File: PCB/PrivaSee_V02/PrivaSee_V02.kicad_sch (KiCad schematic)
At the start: 35 parts, among them J1 RFPC-SMA27-F, J2 Batt_Solder_Point, J3 Conn_02x06_Odd_Even, J4 VOUT_TEST, J5 GND_TEST, J6 IR_TEST, J7 RF_TEST, SW1 Switch, SW2 SW_Push, U1 RC1602A, U2 LM358, U3 254, U4 DFR0568, U6 ESP32-C5-DevKitC-1

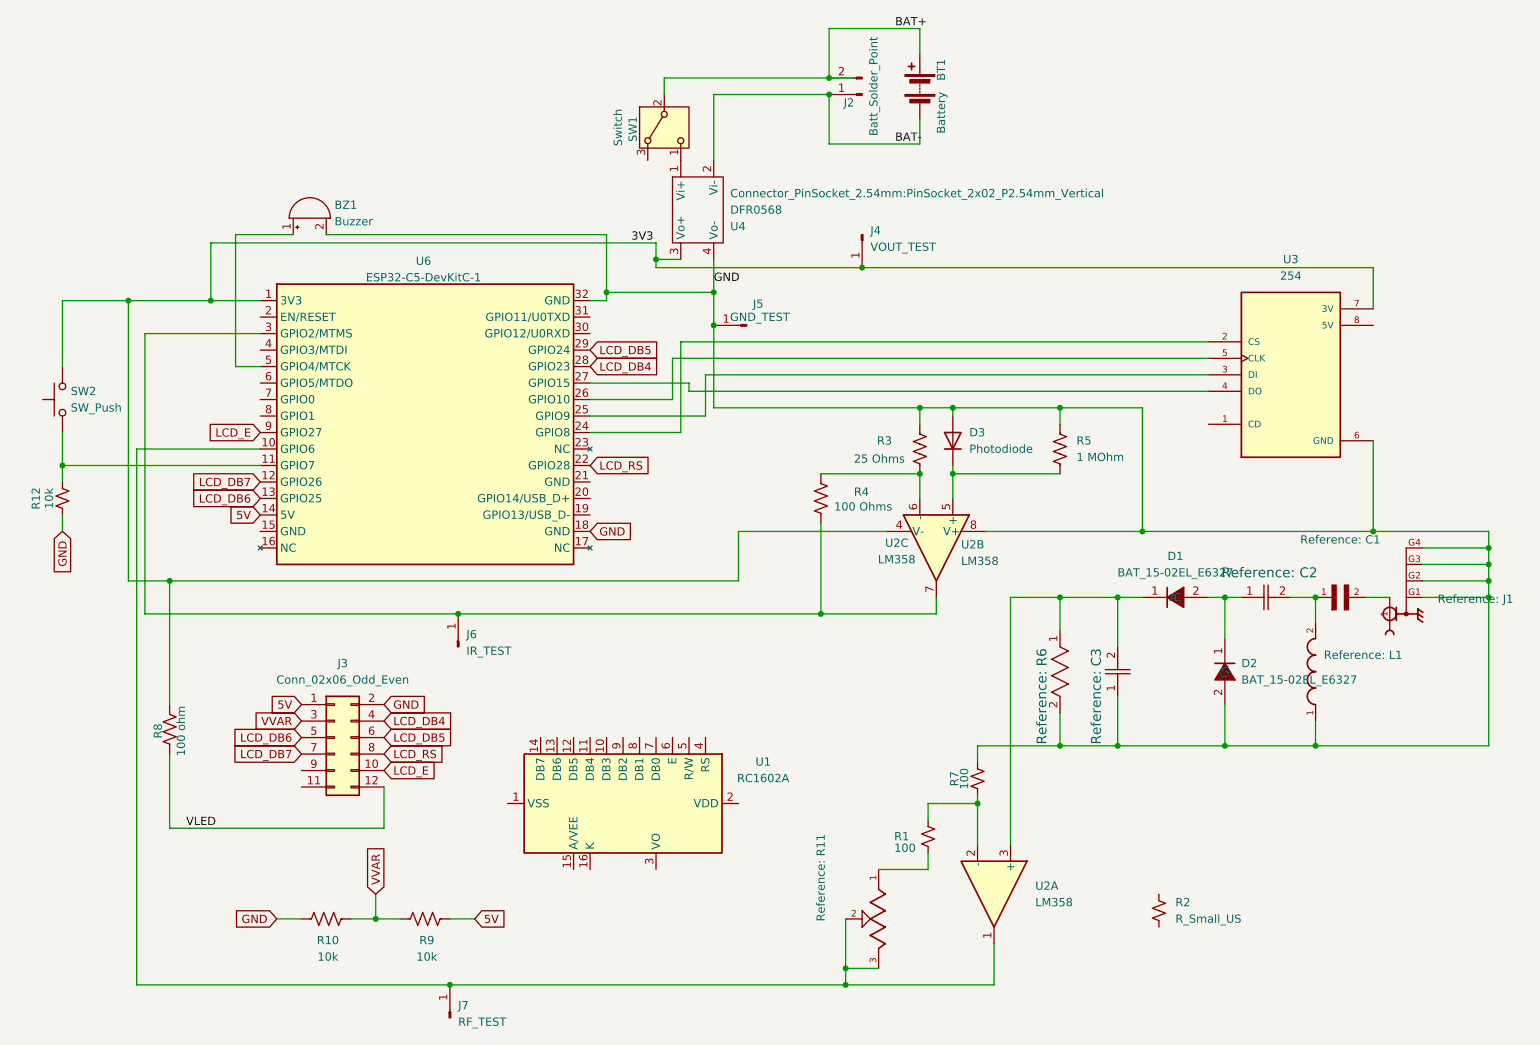
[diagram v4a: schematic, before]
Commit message: capacitor replacement
handsolderable foot print
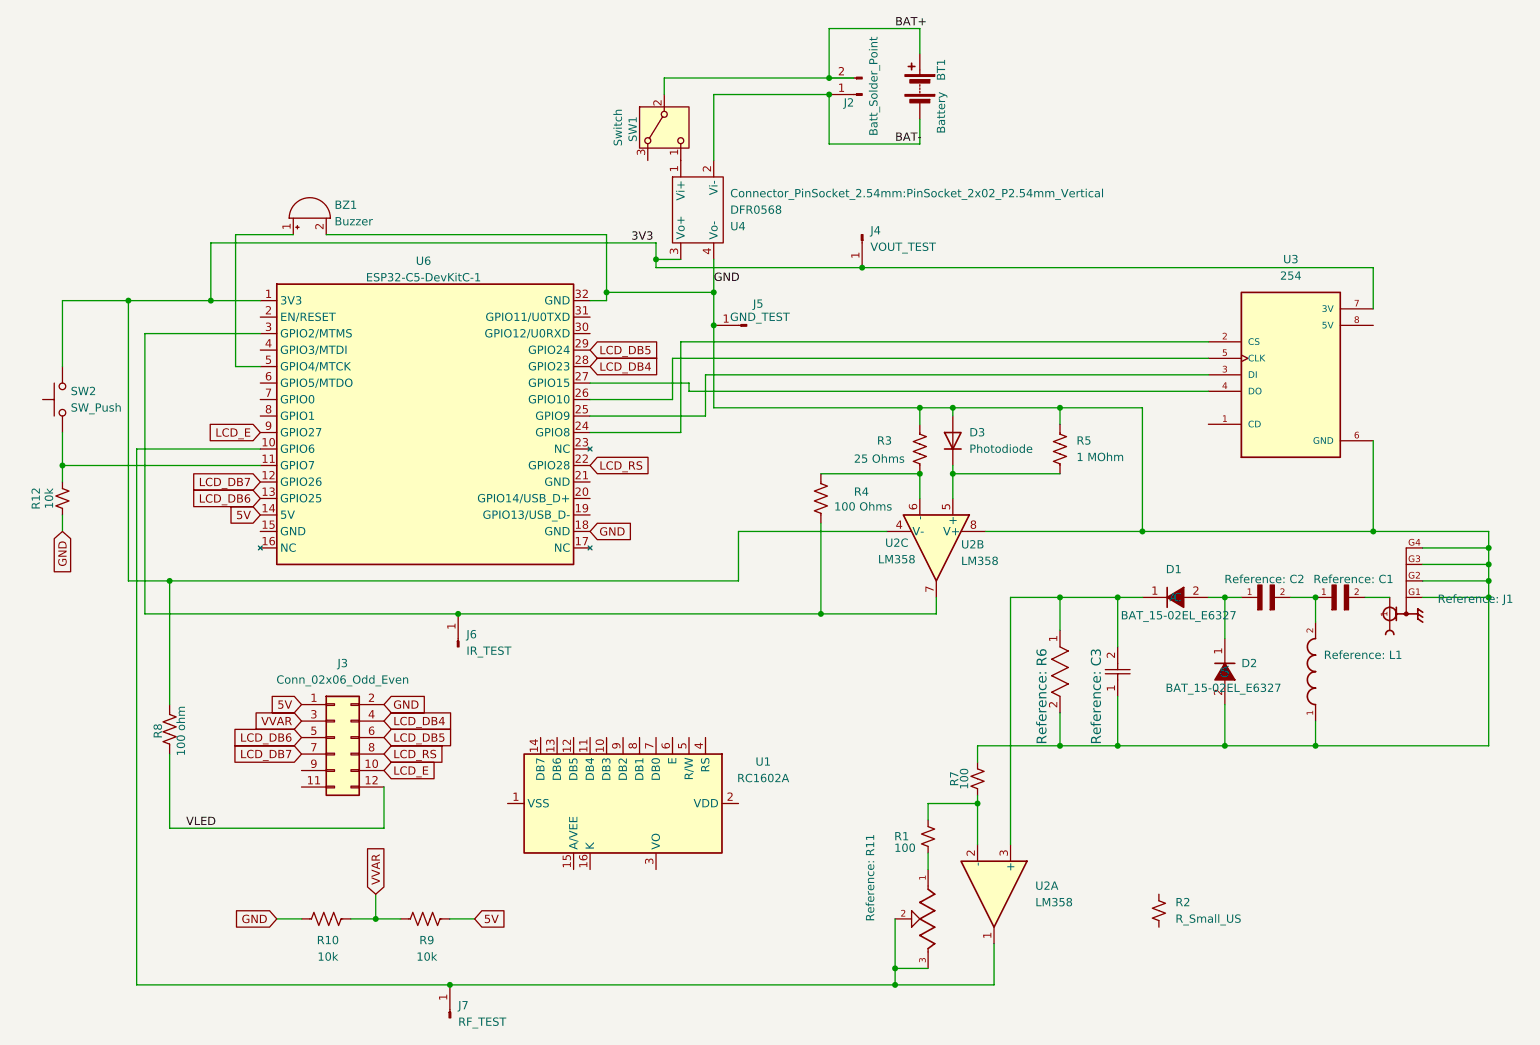
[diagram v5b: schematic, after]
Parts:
- removed C2: GJM1555C1H4R7CB01D, Snapeda:G-155_MUR-L, symbol Snapeda:GJM1555C1H4R7CB01D
- added C2: GJM1555C1H4R7BB01D, Snapeda:CAPC1005X55N, symbol Snapeda:GJM1555C1H4R7BB01D
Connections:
- net at D1.2 (A), D2.1 (C): now also C2.1
- net at C1.1, L1.2: now also C2.2
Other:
- moved on the sheet: Reference: R11
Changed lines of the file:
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@@
 	)
 	(junction
-		(at 154.94 162.56)
-		(diameter 0)
-		(color 0 0 0 0)
-	)
-	(junction
 		(at 213.36 102.87)
 		(diameter 0)
@@
 	)
 	(junction
-		(at 154.94 160.02)
+		(at 44.45 57.15)
 		(diameter 0)
 		(color 0 0 0 0)
 	)
 	(junction
-		(at 44.45 57.15)
+		(at 162.56 160.02)
 		(diameter 0)
 		(color 0 0 0 0)
@@
 		(color 0 0 0 0)
 	)
+	(junction
+		(at 162.56 162.56)
+		(diameter 0)
+		(color 0 0 0 0)
+	)
 	(wire
 		(pts
@@
 	(wire
 		(pts
-			(xy 154.94 160.02) (xy 154.94 162.56)
+			(xy 162.56 160.02) (xy 162.56 162.56)
 		)
 		(stroke
@@
 	(wire
 		(pts
-			(xy 134.62 50.8) (xy 134.62 55.88)
+			(xy 162.56 160.02) (xy 167.64 160.02)
 		)
 		(stroke
@@
 	(wire
 		(pts
-			(xy 166.37 15.24) (xy 152.4 15.24)
+			(xy 134.62 50.8) (xy 134.62 55.88)
 		)
 		(stroke
@@
 	(wire
 		(pts
-			(xy 134.62 55.88) (xy 134.62 60.96)
+			(xy 166.37 15.24) (xy 152.4 15.24)
 		)
 		(stroke
@@
 	(wire
 		(pts
-			(xy 167.64 134.62) (xy 167.64 137.16)
+			(xy 134.62 55.88) (xy 134.62 60.96)
 		)
 		(stroke
@@
 	(wire
 		(pts
-			(xy 118.11 46.99) (xy 118.11 55.88)
+			(xy 167.64 134.62) (xy 167.64 137.16)
 		)
 		(stroke
@@
 	(wire
 		(pts
-			(xy 133.35 74.93) (xy 115.57 74.93)
+			(xy 118.11 46.99) (xy 118.11 55.88)
 		)
 		(stroke
@@
 	(wire
 		(pts
-			(xy 154.94 152.4) (xy 154.94 160.02)
+			(xy 133.35 74.93) (xy 115.57 74.93)
 		)
 		(stroke
@@
 	(wire
 		(pts
-			(xy 168.91 105.41) (xy 168.91 102.87)
+			(xy 162.56 152.4) (xy 162.56 160.02)
 		)
 		(stroke
@@
 	(wire
 		(pts
-			(xy 45.72 80.01) (xy 45.72 162.56)
+			(xy 168.91 105.41) (xy 168.91 102.87)
 		)
 		(stroke
@@
 	(wire
 		(pts
-			(xy 160.02 144.78) (xy 167.64 144.78)
+			(xy 45.72 80.01) (xy 45.72 162.56)
 		)
 		(stroke
@@
 	(wire
 		(pts
-			(xy 154.94 162.56) (xy 177.8 162.56)
-		)
-		(stroke
-			(width 0)
-			(type default)
-		)
-	)
-	(wire
-		(pts
 			(xy 187.96 107.95) (xy 187.96 102.87)
 		)
@@
 	(wire
 		(pts
-			(xy 93.98 162.56) (xy 154.94 162.56)
+			(xy 93.98 162.56) (xy 162.56 162.56)
 		)
 		(stroke
@@
 	(wire
 		(pts
+			(xy 162.56 162.56) (xy 177.8 162.56)
+		)
+		(stroke
+			(width 0)
+			(type default)
+		)
+	)
+	(wire
+		(pts
 			(xy 151.13 83.82) (xy 166.37 83.82)
 		)
@@
 	(wire
 		(pts
-			(xy 154.94 160.02) (xy 160.02 160.02)
-		)
-		(stroke
-			(width 0)
-			(type default)
-		)
-	)
-	(wire
-		(pts
 			(xy 236.22 92.71) (xy 200.66 92.71)
 		)
@@
 		(in_pos_files yes)
 		(dnp no)
-		(fields_autoplaced yes)
 		(property "Reference" "D1"
-			(at 205.74 96.52 0)
+			(at 205.486 98.552 0)
 			(show_name no)
 			(do_not_autoplace no)
@@
 		)
 		(property "Value" "BAT_15-02EL_E6327"
-			(at 205.74 99.06 0)
+			(at 206.248 105.664 0)
 			(show_name no)
 			(do_not_autoplace no)
@@
 		(in_pos_files yes)
 		(dnp no)
-		(fields_autoplaced yes)
 		(property "Reference" "D2"
 			(at 215.9 113.0299 90)
@@
 		)
 		(property "Value" "BAT_15-02EL_E6327"
-			(at 215.9 115.5699 90)
+			(at 204.216 116.84 90)
 			(show_name no)
 			(do_not_autoplace no)
@@
 	)
 	(symbol
-		(lib_id "Snapeda:GJM1555C1H4R7CB01D")
-		(at 215.9 102.87 0)
-		(unit 1)
-		(body_style 1)
-		(exclude_from_sim no)
-		(in_bom yes)
-		(on_board yes)
-		(in_pos_files yes)
-		(dnp no)
-		(property "Reference" "C2"
-			(at 220.218 99.06 0)
-			(show_name yes)
-			(do_not_autoplace no)
-			(effects
-				(font
-					(size 1.524 1.524)
-				)
-			)
-		)
-		(property "Value" "GJM1555C1H4R7CB01D"
-			(at 221.996 100.33 0)
-			(hide yes)
-			(show_name yes)
-			(do_not_autoplace no)
-			(effects
-				(font
-					(size 1.524 1.524)
-				)
-			)
-		)
-		(property "Footprint" "Snapeda:G-155_MUR-L"
-			(at 219.71 96.52 0)
-			(hide yes)
-			(show_name yes)
-			(do_not_autoplace no)
-			(effects
-				(font
-					(size 1.27 1.27)
-				)
-			)
-		)
-		(property "Datasheet" "GJM1555C1H4R7CB01D"
-			(at 219.71 99.06 0)
-			(hide yes)
-			(show_name yes)
-			(do_not_autoplace no)
-			(effects
-				(font
-					(size 1.27 1.27)
-				)
-			)
-		)
-		(property "Description" ""
-			(at 215.9 102.87 0)
-			(hide yes)
-			(show_name yes)
-			(do_not_autoplace no)
-			(effects
-				(font
-					(size 1.27 1.27)
-				)
-			)
-		)
-		(pin "1"
-		)
-		(pin "2"
-		)
-		(instances
-			(project "PrivaSee_V02"
-				(path "/e2eea558-d7b1-4123-919c-3783d093c9eb"
-					(reference "C2")
-					(unit 1)
-				)
-			)
-		)
-	)
-	(symbol
 		(lib_id "Device:R_US")
 		(at 90.17 152.4 90)
@@
 	(symbol
 		(lib_id "Snapeda:3310Y-001-103L")
-		(at 160.02 152.4 270)
+		(at 167.64 152.4 270)
 		(unit 1)
 		(body_style 1)
@@
 		(dnp no)
 		(property "Reference" "R11"
-			(at 151.13 146.05 0)
+			(at 158.75 146.05 0)
 			(show_name yes)
 			(do_not_autoplace no)
@@
 		)
 		(property "Value" "3310Y-001-103L"
-			(at 171.45 152.4 0)
+			(at 179.07 152.4 0)
 			(hide yes)
 			(show_name yes)
@@
 		)
 		(property "Footprint" "Snapeda:TRIM_3310Y-001-103L"
-			(at 168.91 152.4 0)
+			(at 176.53 152.4 0)
 			(hide yes)
 			(show_name yes)
@@
 		)
 		(property "Datasheet" ""
-			(at 156.972 150.876 0)
+			(at 164.592 150.876 0)
 			(hide yes)
 			(show_name yes)
@@
 		)
 		(property "Description" ""
-			(at 157.226 151.638 0)
+			(at 164.846 151.638 0)
 			(hide yes)
 			(show_name yes)
@@
 		)
 		(property "STANDARD" "IPC 7351B"
-			(at 166.37 152.4 0)
+			(at 173.99 152.4 0)
 			(hide yes)
 			(show_name yes)
@@
 		)
 		(property "MANUFACTURER" "BOURNS"
-			(at 163.83 152.4 0)
+			(at 171.45 152.4 0)
 			(hide yes)
 			(show_name yes)
@@
 	)
 	(symbol
+		(lib_id "Snapeda:GJM1555C1H4R7BB01D")
+		(at 218.44 102.87 0)
+		(unit 1)
+		(body_style 1)
+		(exclude_from_sim no)
+		(in_bom yes)
+		(on_board yes)
+		(in_pos_files yes)
+		(dnp no)
+		(property "Reference" "C2"
+			(at 219.456 100.076 0)
+			(show_name yes)
+			(do_not_autoplace no)
+			(effects
+				(font
+					(size 1.27 1.27)
+				)
+			)
+		)
+		(property "Value" "GJM1555C1H4R7BB01D"
+			(at 219.71 96.52 0)
+			(hide yes)
+			(show_name yes)
+			(do_not_autoplace no)
+			(effects
+				(font
+					(size 1.27 1.27)
+				)
+			)
+		)
+		(property "Footprint" "Snapeda:CAPC1005X55N"
+			(at 219.71 99.06 0)
+			(hide yes)
+			(show_name yes)
+			(do_not_autoplace no)
+			(effects
+				(font
+					(size 1.27 1.27)
+				)
+			)
+		)
+		(property "Datasheet" ""
+			(at 218.44 102.87 0)
+			(hide yes)
+			(show_name yes)
+			(do_not_autoplace no)
+			(effects
+				(font
+					(size 1.27 1.27)
+				)
+			)
+		)
+		(property "Description" ""
+			(at 218.44 102.87 0)
+			(hide yes)
+			(show_name yes)
+			(do_not_autoplace no)
+			(effects
+				(font
+					(size 1.27 1.27)
+				)
+			)
+		)
+		(pin "2"
+		)
+		(pin "1"
+		)
+		(instances
+			(project "PrivaSee_V02"
+				(path "/e2eea558-d7b1-4123-919c-3783d093c9eb"
+					(reference "C2")
+					(unit 1)
+				)
+			)
+		)
+	)
+	(symbol
 		(lib_id "Switch:SW_Nidec_CAS-120A1")
 		(at 127 30.48 90)
@@
 		(in_pos_files yes)
 		(dnp no)
-		(fields_autoplaced yes)
 		(property "Reference" "C1"
-			(at 231.14 93.98 0)
+			(at 233.172 100.076 0)
 			(show_name yes)
 			(do_not_autoplace no)

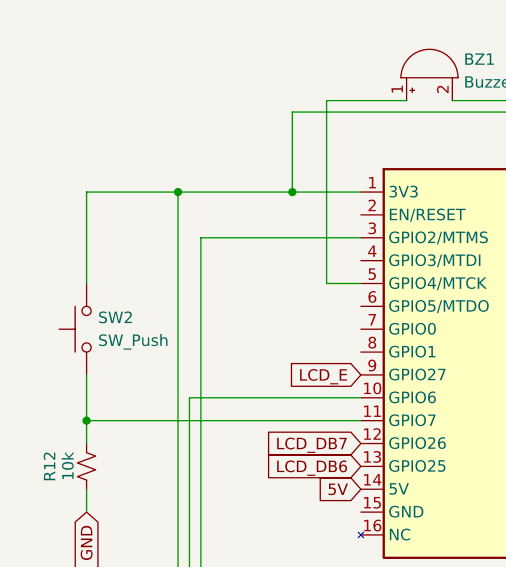
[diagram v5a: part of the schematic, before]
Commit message: button replacement
SPST NO implemented
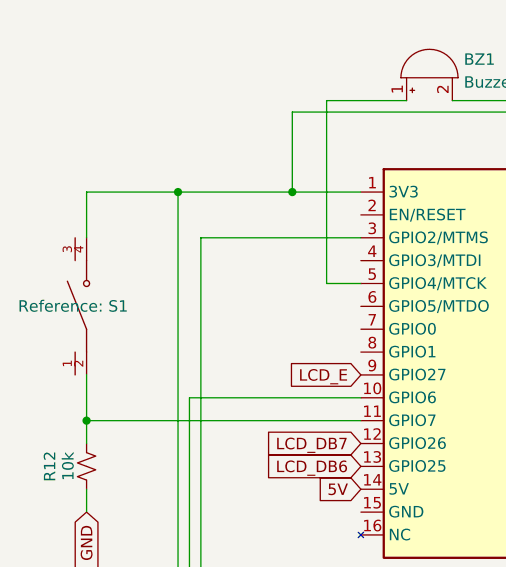
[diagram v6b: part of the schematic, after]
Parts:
- removed SW2: SW_Push, Button_Switch_THT:SW_PUSH_6mm_H4.3mm, symbol Switch:SW_Push
- added S1: D6R90_F2_LFS, Snapeda:SW_D6R90_F2_LFS, symbol Snapeda:D6R90_F2_LFS
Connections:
- net 3V3: now also S1.4
- net at R12.2, U6.11 (GPIO7): now also S1.2
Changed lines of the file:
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@@
 	)
 	(junction
-		(at 162.56 160.02)
+		(at 34.29 82.55)
 		(diameter 0)
 		(color 0 0 0 0)
 	)
 	(junction
-		(at 125.73 50.8)
+		(at 162.56 160.02)
 		(diameter 0)
 		(color 0 0 0 0)
 	)
 	(junction
-		(at 34.29 82.55)
+		(at 125.73 50.8)
 		(diameter 0)
 		(color 0 0 0 0)
@@
 	(wire
 		(pts
-			(xy 34.29 77.47) (xy 34.29 82.55)
-		)
-		(stroke
-			(width 0)
-			(type default)
-		)
-	)
-	(wire
-		(pts
 			(xy 175.26 125.73) (xy 175.26 128.27)
 		)
@@
 	(wire
 		(pts
+			(xy 34.29 57.15) (xy 34.29 62.23)
+		)
+		(stroke
+			(width 0)
+			(type default)
+		)
+	)
+	(wire
+		(pts
 			(xy 46.99 62.23) (xy 64.77 62.23)
 		)
@@
 	(wire
 		(pts
-			(xy 213.36 109.22) (xy 213.36 102.87)
+			(xy 34.29 77.47) (xy 34.29 82.55)
 		)
 		(stroke
@@
 	(wire
 		(pts
-			(xy 34.29 67.31) (xy 34.29 57.15)
+			(xy 213.36 109.22) (xy 213.36 102.87)
 		)
 		(stroke
@@
 	)
 	(symbol
-		(lib_id "Switch:SW_Push")
-		(at 34.29 72.39 90)
-		(unit 1)
-		(body_style 1)
-		(exclude_from_sim no)
-		(in_bom yes)
-		(on_board yes)
-		(in_pos_files yes)
-		(dnp no)
-		(property "Reference" "SW2"
-			(at 35.56 71.1199 90)
-			(show_name no)
-			(do_not_autoplace no)
-			(effects
-				(font
-					(size 1.27 1.27)
-				)
-				(justify right)
-			)
-		)
-		(property "Value" "SW_Push"
-			(at 35.56 73.6599 90)
-			(show_name no)
-			(do_not_autoplace no)
-			(effects
-				(font
-					(size 1.27 1.27)
-				)
-				(justify right)
-			)
-		)
-		(property "Footprint" "Button_Switch_THT:SW_PUSH_6mm_H4.3mm"
-			(at 29.21 72.39 0)
-			(hide yes)
-			(show_name no)
-			(do_not_autoplace no)
-			(effects
-				(font
-					(size 1.27 1.27)
-				)
-			)
-		)
-		(property "Datasheet" ""
-			(at 29.21 72.39 0)
-			(hide yes)
-			(show_name no)
-			(do_not_autoplace no)
-			(effects
-				(font
-					(size 1.27 1.27)
-				)
-			)
-		)
-		(property "Description" "Push button switch, generic, two pins"
-			(at 34.29 72.39 0)
-			(hide yes)
-			(show_name no)
-			(do_not_autoplace no)
-			(effects
-				(font
-					(size 1.27 1.27)
-				)
-			)
-		)
-		(pin "2"
-		)
-		(pin "1"
-		)
-		(instances
-			(project "PrivaSee_V02"
-				(path "/e2eea558-d7b1-4123-919c-3783d093c9eb"
-					(reference "SW2")
-					(unit 1)
-				)
-			)
-		)
-	)
-	(symbol
 		(lib_id "Device:R_US")
 		(at 187.96 80.01 0)
@@
 					(unit 1)
 				)
+			)
+		)
+	)
+	(symbol
+		(lib_id "Snapeda:D6R90_F2_LFS")
+		(at 34.29 69.85 90)
+		(unit 1)
+		(body_style 1)
+		(exclude_from_sim no)
+		(in_bom yes)
+		(on_board yes)
+		(in_pos_files yes)
+		(dnp no)
+		(property "Reference" "S1"
+			(at 26.67 69.85 90)
+			(show_name yes)
+			(do_not_autoplace no)
+			(effects
+				(font
+					(size 1.27 1.27)
+				)
+				(justify right)
+			)
+		)
+		(property "Value" "D6R90_F2_LFS"
+			(at 16.51 69.85 0)
+			(hide yes)
+			(show_name yes)
+			(do_not_autoplace no)
+			(effects
+				(font
+					(size 1.27 1.27)
+				)
+			)
+		)
+		(property "Footprint" "Snapeda:SW_D6R90_F2_LFS"
+			(at 19.05 69.85 0)
+			(hide yes)
+			(show_name yes)
+			(do_not_autoplace no)
+			(effects
+				(font
+					(size 1.27 1.27)
+				)
+			)
+		)
+		(property "Datasheet" ""
+			(at 34.29 69.85 0)
+			(hide yes)
+			(show_name yes)
+			(do_not_autoplace no)
+			(effects
+				(font
+					(size 1.27 1.27)
+				)
+			)
+		)
+		(property "Description" ""
+			(at 34.29 69.85 0)
+			(hide yes)
+			(show_name yes)
+			(do_not_autoplace no)
+			(effects
+				(font
+					(size 1.27 1.27)
+				)
+			)
+		)
+		(property "PARTREV" "21 Feb 22"
+			(at 21.59 69.85 0)
+			(hide yes)
+			(show_name yes)
+			(do_not_autoplace no)
+			(effects
+				(font
+					(size 1.27 1.27)
+				)
+			)
+		)
+		(property "MANUFACTURER" "C&K"
+			(at 24.13 69.85 0)
+			(hide yes)
+			(show_name yes)
+			(do_not_autoplace no)
+			(effects
+				(font
+					(size 1.27 1.27)
+				)
+			)
+		)
+		(property "MAXIMUM_PACKAGE_HEIGHT" "11.3mm"
+			(at 26.67 69.85 0)
+			(hide yes)
+			(show_name yes)
+			(do_not_autoplace no)
+			(effects
+				(font
+					(size 1.27 1.27)
+				)
+			)
+		)
+		(property "STANDARD" "Manufacturer Recommendations"
+			(at 29.21 69.85 0)
+			(hide yes)
+			(show_name yes)
+			(do_not_autoplace no)
+			(effects
+				(font
+					(size 1.27 1.27)
+				)
+			)
+		)
+		(pin "3"
+		)
+		(pin "2"
+		)
+		(pin "4"
+		)
+		(pin "1"
+		)
+		(instances
+			(project "PrivaSee_V02"
+				(path "/e2eea558-d7b1-4123-919c-3783d093c9eb"
+					(reference "S1")
+					(unit 1)
+				)

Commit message: button update
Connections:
- net 3V3: now also S1.3
- net at R12.2, S1.2, U6.11 (GPIO7): now also S1.1
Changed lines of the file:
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@@
+	(wire
+		(pts
+			(xy 34.29 57.15) (xy 34.29 62.23)
+		)
+		(stroke
+			(width 0)
+			(type default)
+		)
+	)
 	(wire
 		(pts
@@
 	(wire
 		(pts
+			(xy 34.29 77.47) (xy 34.29 82.55)
+		)
+		(stroke
+			(width 0)
+			(type default)
+		)
+	)
+	(wire
+		(pts
 			(xy 45.72 80.01) (xy 45.72 162.56)
 		)
@@
 	(wire
 		(pts
-			(xy 34.29 57.15) (xy 34.29 62.23)
-		)
-		(stroke
-			(width 0)
-			(type default)
-		)
-	)
-	(wire
-		(pts
 			(xy 46.99 62.23) (xy 64.77 62.23)
 		)
@@
 		)
 		(stroke
-			(width 0)
-			(type default)
-		)
-	)
-	(wire
-		(pts
-			(xy 34.29 77.47) (xy 34.29 82.55)
-		)
-		(stroke
